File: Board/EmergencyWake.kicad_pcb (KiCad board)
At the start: 2 copper layers, 100 x 67 mm, 5 parts

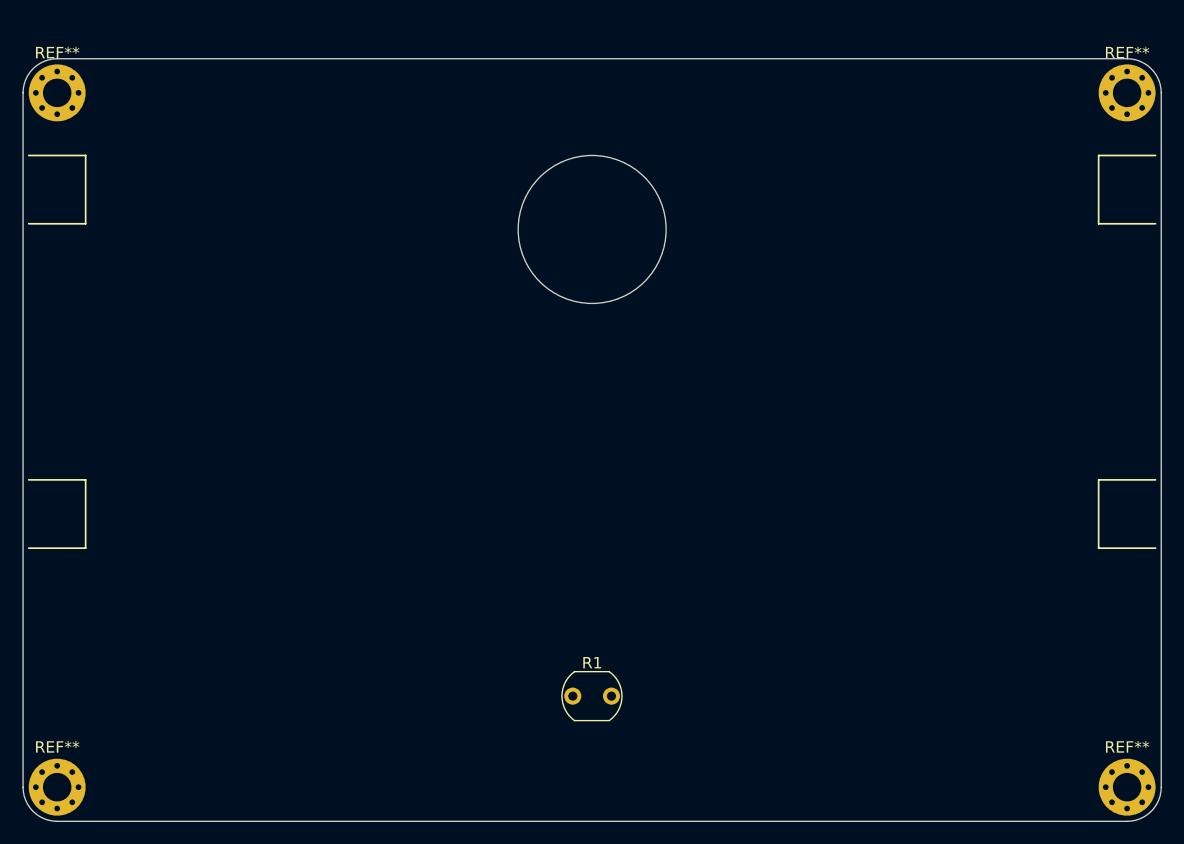
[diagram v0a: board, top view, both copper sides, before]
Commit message: [Board] Added a lot of main components
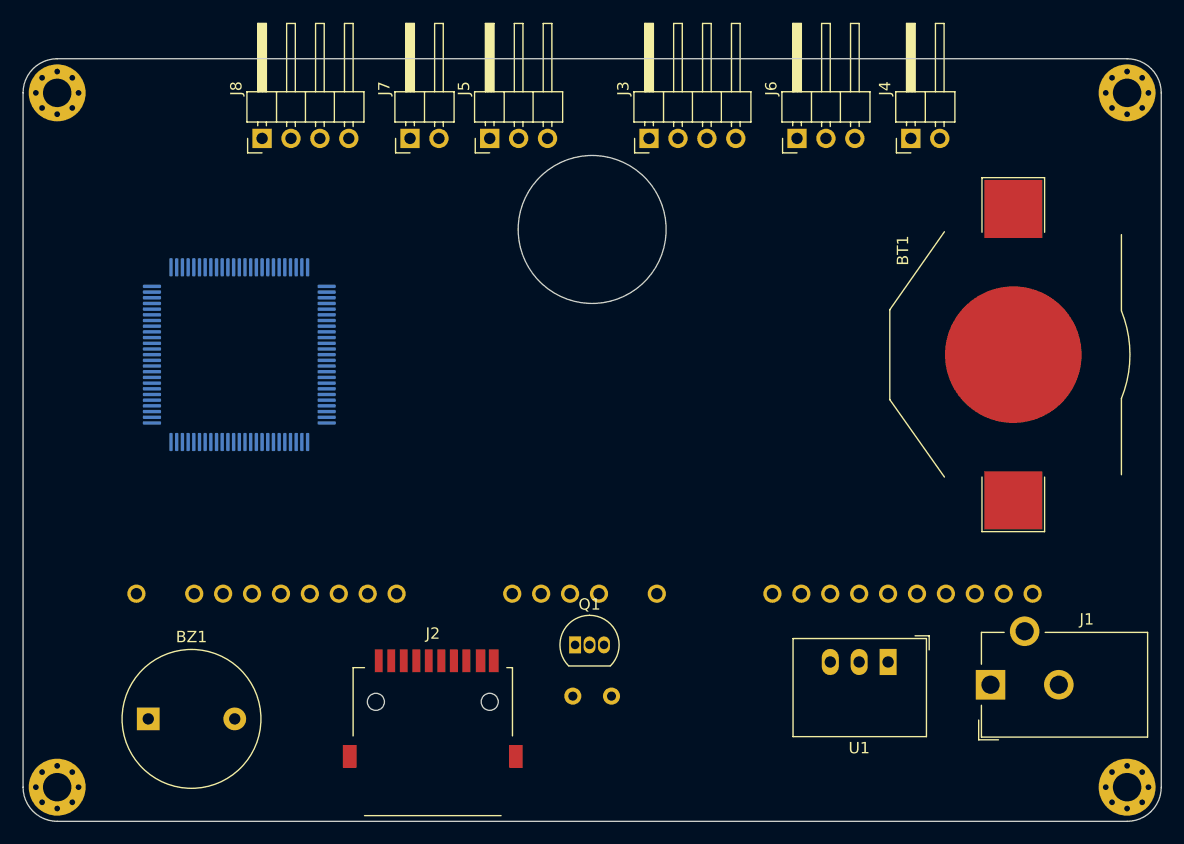
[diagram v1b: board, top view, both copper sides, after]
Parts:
- added BT1: Battery_Cell, Battery:BatteryHolder_Keystone_3002_1x2032, F.Cu at (187.0, 126.0)
- added BZ1: Buzzer, Buzzer_Beeper:Buzzer_12x9.5RM7.6, F.Cu at (111.0, 158.0)
- added D?1: FUTABA_4-LT-46ZB3, VFD:FUTABA_4-LT-46ZB3, B.Cu at (150.0, 126.0)
- added J1: Barrel_Jack_Switch, Connector_BarrelJack:BarrelJack_CUI_PJ-102AH_Horizontal, F.Cu at (185.0, 155.0)
- added J2: Micro_SD_Card_Det, Card:microSD_Attend_112I-TDAR-R 1, F.Cu at (136.0, 156.5)
- added J3: Conn_01x04, Connector_PinHeader_2.54mm:PinHeader_1x04_P2.54mm_Horizontal, F.Cu at (155.0, 107.0)
- added J4: Conn_01x02, Connector_PinHeader_2.54mm:PinHeader_1x02_P2.54mm_Horizontal, F.Cu at (178.0, 107.0)
- added J5: Conn_01x03, Connector_PinHeader_2.54mm:PinHeader_1x03_P2.54mm_Horizontal, F.Cu at (141.0, 107.0)
- added J6: Conn_01x03, Connector_PinHeader_2.54mm:PinHeader_1x03_P2.54mm_Horizontal, F.Cu at (168.0, 107.0)
- added J7: Conn_01x02, Connector_PinHeader_2.54mm:PinHeader_1x02_P2.54mm_Horizontal, F.Cu at (134.0, 107.0)
- added J8: Conn_01x04, Connector_PinHeader_2.54mm:PinHeader_1x04_P2.54mm_Horizontal, F.Cu at (121.0, 107.0)
- added Q1: MPSA13, Package_TO_SOT_THT:TO-92_Inline, F.Cu at (148.5, 151.5)
- added U1: R-78C3.3-1.0, Converter_DCDC:Converter_DCDC_RECOM_R-78E-0.5_THT, F.Cu at (176.0, 153.0)
- added U2: STM32F103VETx, Package_QFP:LQFP-100_14x14mm_P0.5mm, B.Cu at (119.0, 126.0)
- ? (x4): renamed from REF**; value MountingHole_2.5mm_Pad_Via -> (none)
- R1: moved to B.Cu

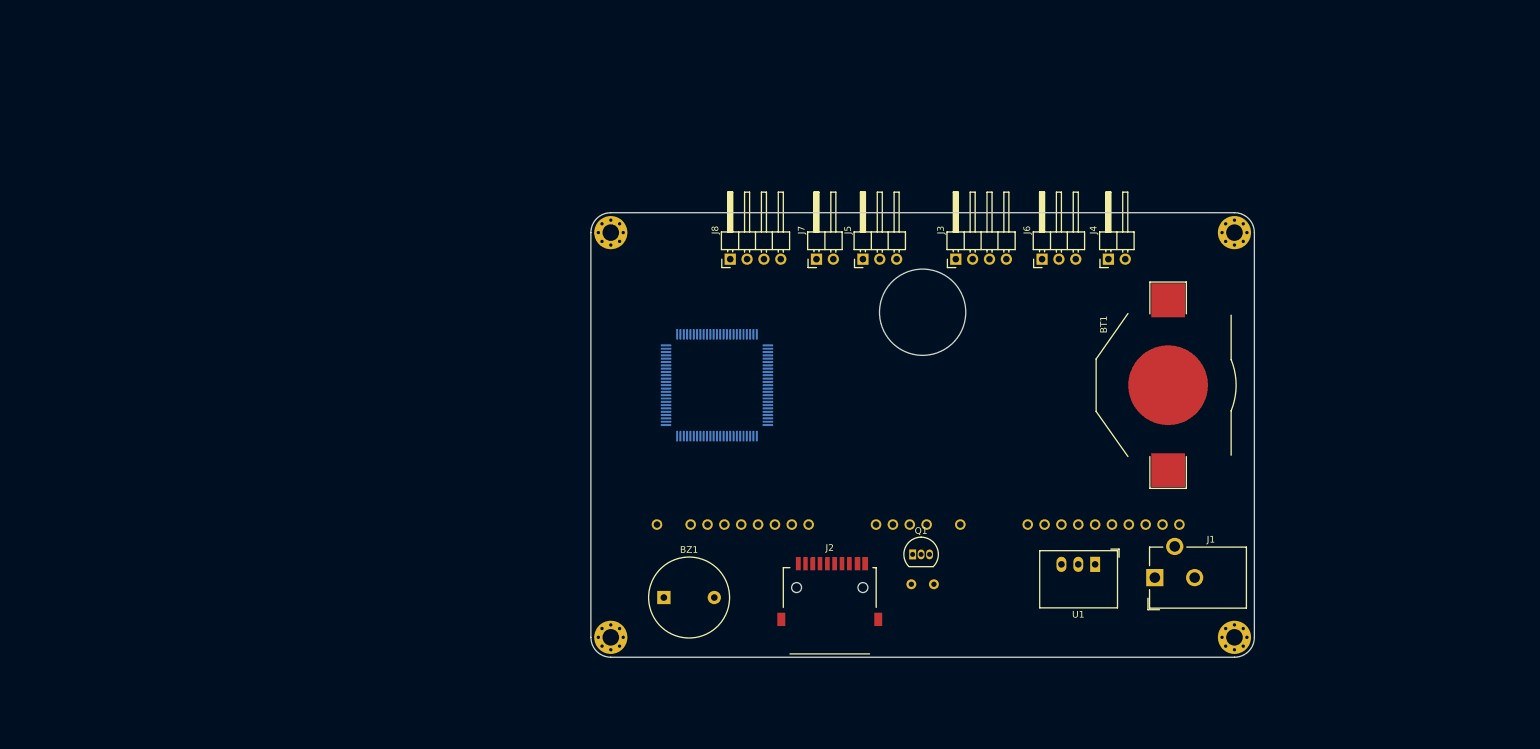
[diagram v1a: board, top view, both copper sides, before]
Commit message: [Board] Added all remaining components, arranged them approximately on PCB
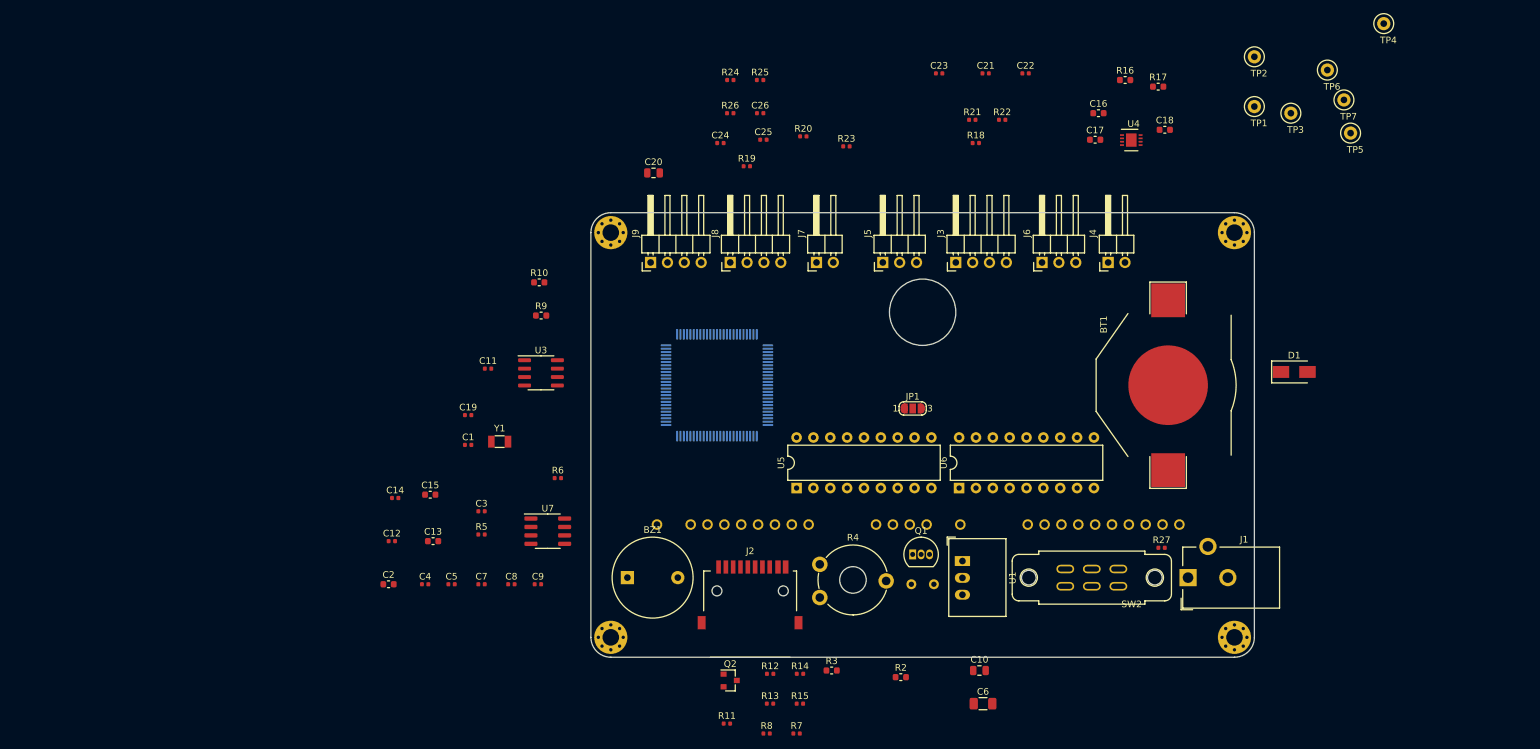
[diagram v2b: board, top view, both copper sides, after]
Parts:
- removed D?1: FUTABA_4-LT-46ZB3, VFD:FUTABA_4-LT-46ZB3
- added C1: 6p, Capacitor_SMD:C_0402_1005Metric, F.Cu at (81.5, 135.0)
- added C10: 22u,25V, Capacitor_SMD:C_0805_2012Metric, F.Cu at (158.6, 169.0)
- added C11: 100n, Capacitor_SMD:C_0402_1005Metric, F.Cu at (84.5, 123.5)
- added C12: 10n,50V, Capacitor_SMD:C_0402_1005Metric, F.Cu at (70.0, 149.5)
- added C13: 1u,50V, Capacitor_SMD:C_0603_1608Metric, F.Cu at (76.2, 149.5)
- added C14: 10n,50V, Capacitor_SMD:C_0402_1005Metric, F.Cu at (70.5, 143.0)
- added C15: 1u,50V, Capacitor_SMD:C_0603_1608Metric, F.Cu at (75.8, 142.5)
- added C16: 10n, Capacitor_SMD:C_0603_1608Metric, F.Cu at (176.5, 85.0)
- added C17: 10n, Capacitor_SMD:C_0603_1608Metric, F.Cu at (176.0, 89.0)
- added C18: 1u,50V, Capacitor_SMD:C_0603_1608Metric, F.Cu at (186.5, 87.5)
- added C19: 6p, Capacitor_SMD:C_0402_1005Metric, F.Cu at (81.5, 130.5)
- added C2: 4u7,16V, Capacitor_SMD:C_0603_1608Metric, F.Cu at (69.5, 156.0)
- added C20: 10u,50V, Capacitor_SMD:C_0805_2012Metric, F.Cu at (109.4, 94.0)
- added C21: 10n,50V, Capacitor_SMD:C_0402_1005Metric, F.Cu at (159.5, 79.0)
- added C22: 10n,50V, Capacitor_SMD:C_0402_1005Metric, F.Cu at (165.5, 79.0)
- added C23: 10n,50V, Capacitor_SMD:C_0402_1005Metric, F.Cu at (152.5, 79.0)
- added C24: 10n,50V, Capacitor_SMD:C_0402_1005Metric, F.Cu at (119.5, 89.5)
- added C25: 10n,50V, Capacitor_SMD:C_0402_1005Metric, F.Cu at (126.0, 89.0)
- added C26: 10n,50V, Capacitor_SMD:C_0402_1005Metric, F.Cu at (125.5, 85.0)
- added C3: 10n,50V, Capacitor_SMD:C_0402_1005Metric, F.Cu at (83.5, 145.0)
- added C4: 100n, Capacitor_SMD:C_0402_1005Metric, F.Cu at (75.0, 156.0)
- added C5: 100n, Capacitor_SMD:C_0402_1005Metric, F.Cu at (79.0, 156.0)
- added C6: 10u,50V, Capacitor_SMD:C_1206_3216Metric, F.Cu at (159.1, 174.0)
- added C7: 100n, Capacitor_SMD:C_0402_1005Metric, F.Cu at (83.5, 156.0)
- added C8: 100n, Capacitor_SMD:C_0402_1005Metric, F.Cu at (88.0, 156.0)
- added C9: 100n, Capacitor_SMD:C_0402_1005Metric, F.Cu at (92.0, 156.0)
- added D1: D_Schottky, Diode_SMD:D_SMA, F.Cu at (206.0, 124.0)
- added DISP1: FUTABA_4-LT-46ZB3, VFD:FUTABA_4-LT-46ZB3, B.Cu at (150.0, 126.0)
- added J9: Conn_01x04, Connector_PinHeader_2.54mm:PinHeader_1x04_P2.54mm_Horizontal, F.Cu at (109.0, 107.5)
- added JP1: SolderJumper_3_Open, Jumper:SolderJumper-3_P1.3mm_Open_RoundedPad1.0x1.5mm_NumberLabels, F.Cu at (148.5, 129.5)
- added Q2: AO3400A, Package_TO_SOT_SMD:SOT-23, F.Cu at (121.0, 170.5)
- added R10: 15k,1%, Resistor_SMD:R_0603_1608Metric, F.Cu at (92.2, 110.5)
- added R11: 100k, Resistor_SMD:R_0402_1005Metric, F.Cu at (120.5, 177.0)
- added R12: 100k, Resistor_SMD:R_0402_1005Metric, F.Cu at (127.0, 169.5)
- added R13: 100k, Resistor_SMD:R_0402_1005Metric, F.Cu at (127.0, 174.0)
- added R14: 100k, Resistor_SMD:R_0402_1005Metric, F.Cu at (131.5, 169.5)
- added R15: 100k, Resistor_SMD:R_0402_1005Metric, F.Cu at (131.5, 174.0)
- added R16: 300k, Resistor_SMD:R_0603_1608Metric, F.Cu at (180.5, 80.0)
- added R17: 300k, Resistor_SMD:R_0603_1608Metric, F.Cu at (185.5, 81.0)
- added R18: 100k, Resistor_SMD:R_0402_1005Metric, F.Cu at (158.0, 89.5)
- added R19: 10k, Resistor_SMD:R_0402_1005Metric, F.Cu at (123.5, 93.0)
- added R2: 27k, Resistor_SMD:R_0603_1608Metric, F.Cu at (146.7, 170.0)
- added R20: 10k, Resistor_SMD:R_0402_1005Metric, F.Cu at (132.0, 88.5)
- added R21: 100k, Resistor_SMD:R_0402_1005Metric, F.Cu at (157.5, 86.0)
- added R22: 100k, Resistor_SMD:R_0402_1005Metric, F.Cu at (162.0, 86.0)
- added R23: 100k, Resistor_SMD:R_0402_1005Metric, F.Cu at (138.5, 90.0)
- added R24: 100k, Resistor_SMD:R_0402_1005Metric, F.Cu at (121.0, 80.0)
- added R25: 100k, Resistor_SMD:R_0402_1005Metric, F.Cu at (125.5, 80.0)
- added R26: 100k, Resistor_SMD:R_0402_1005Metric, F.Cu at (121.0, 85.0)
- added R27: 100k, Resistor_SMD:R_0402_1005Metric, F.Cu at (186.0, 150.5)
- added R3: 4k7, Resistor_SMD:R_0603_1608Metric, F.Cu at (136.3, 169.0)
- added R4: 10k, Potentiometer_THT:Potentiometer_Piher_PT-10-V10_Vertical_Hole, F.Cu at (134.5, 158.0)
- added R5: 100k, Resistor_SMD:R_0402_1005Metric, F.Cu at (83.5, 148.5)
- added R6: 100k, Resistor_SMD:R_0402_1005Metric, F.Cu at (95.0, 140.0)
- added R7: 100k, Resistor_SMD:R_0402_1005Metric, F.Cu at (131.0, 178.5)
- added R8: 100k, Resistor_SMD:R_0402_1005Metric, F.Cu at (126.5, 178.5)
- added R9: 82k,1%, Resistor_SMD:R_0603_1608Metric, F.Cu at (92.5, 115.5)
- added SW2: SW_DPDT_x2, Switch:SlidingSwitch_6pin, F.Cu at (175.5, 155.0)
- added TP1: TestPoint, TestPoint:TestPoint_Loop_D1.80mm_Drill1.0mm_Beaded, F.Cu at (200.0, 84.0)
- added TP2: TestPoint, TestPoint:TestPoint_Loop_D1.80mm_Drill1.0mm_Beaded, F.Cu at (200.0, 76.5)
- added TP3: TestPoint, TestPoint:TestPoint_Loop_D1.80mm_Drill1.0mm_Beaded, F.Cu at (205.5, 85.0)
- added TP4: TestPoint, TestPoint:TestPoint_Loop_D1.80mm_Drill1.0mm_Beaded, F.Cu at (219.5, 71.5)
- added TP5: TestPoint, TestPoint:TestPoint_Loop_D1.80mm_Drill1.0mm_Beaded, F.Cu at (214.5, 88.0)
- added TP6: TestPoint, TestPoint:TestPoint_Loop_D1.80mm_Drill1.0mm_Beaded, F.Cu at (211.0, 78.5)
- added TP7: TestPoint, TestPoint:TestPoint_Loop_D1.80mm_Drill1.0mm_Beaded, F.Cu at (213.5, 83.0)
- added U3: M24C02-WMN, Package_SO:SOIC-8_3.9x4.9mm_P1.27mm, F.Cu at (92.5, 124.1)
- added U4: LM4670, Package_SON:WSON-8-1EP_3x3mm_P0.5mm_EP1.6x2.0mm, F.Cu at (181.4, 89.0)
- added U5: UDN6118A, Package_DIP:DIP-18_W7.62mm, F.Cu at (131.0, 141.5)
- added U6: UDN6118A, Package_DIP:DIP-18_W7.62mm, F.Cu at (155.5, 141.5)
- added U7: L9110S, Package_SO:SOP-8_3.76x4.96mm_P1.27mm, F.Cu at (93.5, 148.0)
- added Y1: 32,768, Crystal:Crystal_SMD_3215-2Pin_3.2x1.5mm, F.Cu at (86.2, 134.5)
- R1: value LDR07 -> GL5506
- U1: value R-78C3.3-1.0 -> Gaptec LME78_03-1.0
- moved U1 20.0 mm to (156.0, 152.5), turned to 270 degrees
- moved J2 12.0 mm to (124.0, 157.0)
- moved BZ1 6.26 mm to (105.5, 155.0)
- moved J1 5.00 mm to (190.0, 155.0)
- moved J5 3.04 mm to (144.0, 107.5)
- moved J4 0.50 mm to (178.0, 107.5)
- moved J3 0.50 mm to (155.0, 107.5)
- moved J6 0.50 mm to (168.0, 107.5)
- moved J7 0.50 mm to (134.0, 107.5)
- moved J8 0.50 mm to (121.0, 107.5)
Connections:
- net Net-(BZ1-Pad1) renamed /BUZZER
- net Net-(J2-Pad9) renamed /CARD_DET
- net Net-(J3-Pad2) renamed /SWCLK
- net Net-(J3-Pad3) renamed /SWDIO
- net Net-(J5-Pad1) renamed /UART_TX
- net Net-(J5-Pad2) renamed /UART_RX
- BT1 pad 1: Net-(BT1-Pad1) -> +3V0
- BT1 pad 2: Net-(BT1-Pad2) -> GND
- BZ1 pad 2: Net-(BZ1-Pad2) -> GND
- J1 pad 2: Net-(J1-Pad2) -> GND
- J2 pad 10: Net-(J2-Pad10) -> GND
- J2 pad 11: Net-(J2-Pad11) -> GND
- J2 pad 4: Net-(J2-Pad4) -> VCC
- J3 pad 1: Net-(J3-Pad1) -> VCC
- J3 pad 4: Net-(J3-Pad4) -> GND
- J4 pad 1: Net-(J4-Pad1) -> /SP+
- J4 pad 2: Net-(J4-Pad2) -> /SP-
- J5 pad 3: Net-(J5-Pad3) -> GND
- J6 pad 1: Net-(J6-Pad1) -> /TOGGLE_UP
- J6 pad 2: Net-(J6-Pad2) -> /TOGGLE_DOWN
- J6 pad 3: Net-(J6-Pad3) -> GND
- J7 pad 1: Net-(J7-Pad1) -> /LEVER
- J7 pad 2: Net-(J7-Pad2) -> GND
- J8 pad 3: Net-(J8-Pad3) -> /ENC_BUT
- J8 pad 4: Net-(J8-Pad4) -> GND
- Q1 pad 1: Net-(Q1-Pad1) -> +VDC
- Q1 pad 3: Net-(Q1-Pad3) -> +24V
- R1 pad 1: Net-(R1-Pad1) -> +24V
- R1 pad 2: Net-(R1-Pad2) -> Net-(Q1-Pad2)
- U1 pad 1: Net-(U1-Pad1) -> +24V
- U1 pad 2: Net-(U1-Pad2) -> GND
- U1 pad 3: Net-(U1-Pad3) -> VCC
- U2 pad 10: Net-(U2-Pad10) -> GND
- U2 pad 100: Net-(U2-Pad100) -> VCC
- U2 pad 11: Net-(U2-Pad11) -> VCC
- U2 pad 14: Net-(U2-Pad14) -> /RESET
- U2 pad 19: Net-(U2-Pad19) -> GND
- U2 pad 20: Net-(U2-Pad20) -> GND
- U2 pad 21: Net-(U2-Pad21) -> VCC
- U2 pad 22: Net-(U2-Pad22) -> VCC
- U2 pad 27: Net-(U2-Pad27) -> GND
- U2 pad 28: Net-(U2-Pad28) -> VCC
- U2 pad 49: Net-(U2-Pad49) -> GND
- U2 pad 50: Net-(U2-Pad50) -> VCC
- U2 pad 6: Net-(U2-Pad6) -> VCC
- U2 pad 74: Net-(U2-Pad74) -> GND
- U2 pad 75: Net-(U2-Pad75) -> VCC
- U2 pad 94: Net-(U2-Pad94) -> /BOOT0
- U2 pad 99: Net-(U2-Pad99) -> GND
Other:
- outline, holes or cut-outs redrawn

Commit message: [Board] Placed a lot of components!
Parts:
- added C27: 10n,50V, Capacitor_SMD:C_0402_1005Metric, B.Cu at (158.5, 92.5)
- added C28: 10n,50V, Capacitor_SMD:C_0402_1005Metric, B.Cu at (161.5, 92.5)
- added C29: 10n,50V, Capacitor_SMD:C_0402_1005Metric, B.Cu at (164.5, 92.5)
- added C30: 10n,50V, Capacitor_SMD:C_0402_1005Metric, B.Cu at (180.0, 89.0)
- added C31: 10n,50V, Capacitor_SMD:C_0402_1005Metric, B.Cu at (183.5, 89.0)
- added C32: 10n,50V, Capacitor_SMD:C_0402_1005Metric, B.Cu at (186.5, 89.0)
- added D2: white, LED_SMD:LED_0805_2012Metric_Castellated, B.Cu at (106.0, 132.0)
- added D3: white, LED_SMD:LED_0805_2012Metric_Castellated, B.Cu at (194.0, 126.0)
- added D4: white, LED_SMD:LED_0805_2012Metric_Castellated, B.Cu at (194.0, 132.0)
- added D5: SS54, Diode_SMD:D_SMA, B.Cu at (195.0, 147.0)
- added D6: SS54, Diode_SMD:D_SMA, B.Cu at (169.3, 153.5)
- added JP2: SolderJumper_3_Open, Jumper:SolderJumper-3_P1.3mm_Open_RoundedPad1.0x1.5mm_NumberLabels, F.Cu at (125.5, 140.0)
- added JP3: SolderJumper_3_Open, Jumper:SolderJumper-3_P1.3mm_Open_RoundedPad1.0x1.5mm_NumberLabels, F.Cu at (125.5, 143.0)
- added JP4: SolderJumper_3_Open, Jumper:SolderJumper-3_P1.3mm_Open_RoundedPad1.0x1.5mm_NumberLabels, F.Cu at (150.0, 140.0)
- added L1: 33u, Inductor_SMD:L_Wuerth_WE-PD-Typ-7345, B.Cu at (175.3, 154.5)
- added R28: 100k, Resistor_SMD:R_0402_1005Metric, B.Cu at (158.5, 89.5)
- added R29: 100k, Resistor_SMD:R_0402_1005Metric, B.Cu at (161.5, 89.5)
- added R30: 100k, Resistor_SMD:R_0402_1005Metric, B.Cu at (164.5, 89.5)
- added R31: 100k, Resistor_SMD:R_0402_1005Metric, B.Cu at (152.5, 95.0)
- added R32: 100k, Resistor_SMD:R_0402_1005Metric, B.Cu at (184.0, 92.0)
- added R33: 100k, Resistor_SMD:R_0402_1005Metric, B.Cu at (184.0, 94.5)
- added R34: 100k, Resistor_SMD:R_0402_1005Metric, B.Cu at (188.0, 94.5)
- added R35: 390, Resistor_SMD:R_0603_1608Metric, B.Cu at (226.5, 155.5)
- added R36: 390, Resistor_SMD:R_0603_1608Metric, B.Cu at (226.5, 159.5)
- added R37: 10k, Resistor_SMD:R_0603_1608Metric, B.Cu at (123.2, 95.0)
- added R38: 10k, Resistor_SMD:R_0603_1608Metric, B.Cu at (231.5, 155.0)
- added R39: 10k, Resistor_SMD:R_0603_1608Metric, B.Cu at (231.5, 159.0)
- added R40: 100k, Resistor_SMD:R_0402_1005Metric, B.Cu at (185.0, 149.0)
- added SW1: SW_DPDT_x2, Wuerth:452404020202, F.Cu at (184.0, 155.0)
- added SW3: SW_Push, Wuerth:436351045816, F.Cu at (160.0, 165.0)
- added SW4: SW_Push, Wuerth:436351045816, F.Cu at (150.0, 165.0)
- added TP10: -17V, TestPoint:TestPoint_Loop_D1.80mm_Drill1.0mm_Beaded, F.Cu at (21.0, 113.5)
- added TP11: TestPoint, TestPoint:TestPoint_Loop_D1.80mm_Drill1.0mm_Beaded, F.Cu at (17.0, 101.5)
- added TP8: -20V, TestPoint:TestPoint_Loop_D1.80mm_Drill1.0mm_Beaded, F.Cu at (14.5, 107.5)
- added TP9: LDR, TestPoint:TestPoint_Loop_D1.80mm_Drill1.0mm_Beaded, F.Cu at (150.0, 152.0)
- added U10: L9110S, Package_SO:SOP-8_3.76x4.96mm_P1.27mm, B.Cu at (233.5, 146.5)
- added U8: EL357N-G, Package_SO:SOP-4_3.8x4.1mm_P2.54mm, B.Cu at (224.5, 151.0)
- added U9: EL357N-G, Package_SO:SOP-4_3.8x4.1mm_P2.54mm, B.Cu at (224.5, 146.0)
- C1: value 6p -> 4u7,16V; footprint Capacitor_SMD:C_0402_1005Metric -> Capacitor_SMD:C_0603_1608Metric; moved to B.Cu
- C10: value 22u,25V -> 10n,50V; footprint Capacitor_SMD:C_0805_2012Metric -> Capacitor_SMD:C_0402_1005Metric; moved to B.Cu
- C11: value 100n -> 10n,50V; moved to B.Cu
- C12, C24, C25: value 10n,50V -> 1u,50V; footprint Capacitor_SMD:C_0402_1005Metric -> Capacitor_SMD:C_0603_1608Metric; moved to B.Cu
- C13: value 1u,50V -> 22u,25V; footprint Capacitor_SMD:C_0603_1608Metric -> Capacitor_SMD:C_0805_2012Metric; moved to B.Cu
- C14: value 10n,50V -> 100u,50V; footprint Capacitor_SMD:C_0402_1005Metric -> Capacitor_THT:CP_Radial_D6.3mm_P2.50mm
- C15: value 1u,50V -> 10n,50V; footprint Capacitor_SMD:C_0603_1608Metric -> Capacitor_SMD:C_0402_1005Metric; moved to B.Cu
- C16: value 10n -> 470p; moved to B.Cu
- C17: value 10n -> 1u,50V; moved to B.Cu
- C18: value 1u,50V -> 33u,63V; footprint Capacitor_SMD:C_0603_1608Metric -> Capacitor_THT:CP_Radial_D6.3mm_P2.50mm
- C19: value 6p -> 10n; footprint Capacitor_SMD:C_0402_1005Metric -> Capacitor_SMD:C_0603_1608Metric; moved to B.Cu
- C2: value 4u7,16V -> 100n; footprint Capacitor_SMD:C_0603_1608Metric -> Capacitor_SMD:C_0402_1005Metric; moved to B.Cu
- C20: value 10u,50V -> 10n; footprint Capacitor_SMD:C_0805_2012Metric -> Capacitor_SMD:C_0603_1608Metric; moved to B.Cu
- C21, C22: value 10n,50V -> 6p; moved to B.Cu
- C23: value 10n,50V -> 100n; moved to B.Cu
- C26: value 10n,50V -> 10u,50V; footprint Capacitor_SMD:C_0402_1005Metric -> Capacitor_SMD:C_0805_2012Metric; moved to B.Cu
- C3, C4, C5, C7, C8, R11, R12, R13, R14, R15, R6, R8, Y1: moved to B.Cu
- C6: value 10u,50V -> 100n; footprint Capacitor_SMD:C_1206_3216Metric -> Capacitor_SMD:C_0402_1005Metric; moved to B.Cu
- C9: value 100n -> 10u,50V; footprint Capacitor_SMD:C_0402_1005Metric -> Capacitor_SMD:C_1206_3216Metric; moved to B.Cu
- D1: value D_Schottky -> white; footprint Diode_SMD:D_SMA -> LED_SMD:LED_0805_2012Metric_Castellated; moved to B.Cu
- J1: value Barrel_Jack_Switch -> USB_C_Plug_USB2.0; footprint Connector_BarrelJack:BarrelJack_CUI_PJ-102AH_Horizontal -> Wuerth:632723300011
- J3: value Conn_01x04 -> Conn_01x03; footprint Connector_PinHeader_2.54mm:PinHeader_1x04_P2.54mm_Horizontal -> Connector_PinHeader_2.54mm:PinHeader_1x03_P2.54mm_Horizontal
- J6: value Conn_01x03 -> Conn_01x04; footprint Connector_PinHeader_2.54mm:PinHeader_1x03_P2.54mm_Horizontal -> Connector_PinHeader_2.54mm:PinHeader_1x04_P2.54mm_Horizontal
- Q1: value MPSA13 -> AO3400A; footprint Package_TO_SOT_THT:TO-92_Inline -> Package_TO_SOT_SMD:SOT-23; moved to B.Cu
- Q2: value AO3400A -> AO3401A; moved to B.Cu
- R1: value GL5506 -> 100k; footprint OptoDevice:R_LDR_5.1x4.3mm_P3.4mm_Vertical -> Resistor_SMD:R_0402_1005Metric
- R10: value 15k,1% -> 100k; footprint Resistor_SMD:R_0603_1608Metric -> Resistor_SMD:R_0402_1005Metric; moved to B.Cu
- R16, R17: value 300k -> 100k; footprint Resistor_SMD:R_0603_1608Metric -> Resistor_SMD:R_0402_1005Metric; moved to B.Cu
- R18: value 100k -> 0.18; footprint Resistor_SMD:R_0402_1005Metric -> Wuerth:561070332057; moved to B.Cu
- R19: value 10k -> 75k; footprint Resistor_SMD:R_0402_1005Metric -> Resistor_SMD:R_0603_1608Metric; moved to B.Cu
- R2: value 27k -> 150; footprint Resistor_SMD:R_0603_1608Metric -> Resistor_SMD:R_0402_1005Metric; moved to B.Cu
- R20: value 10k -> 5.1k; footprint Resistor_SMD:R_0402_1005Metric -> Resistor_SMD:R_0603_1608Metric; moved to B.Cu
- R21, R22: value 100k -> 300k; footprint Resistor_SMD:R_0402_1005Metric -> Resistor_SMD:R_0603_1608Metric; moved to B.Cu
- R23: value 100k -> 20k; footprint Resistor_SMD:R_0402_1005Metric -> Resistor_SMD:R_0603_1608Metric; moved to B.Cu
- R24: value 100k -> GL5516; footprint Resistor_SMD:R_0402_1005Metric -> OptoDevice:R_LDR_5.1x4.3mm_P3.4mm_Vertical; moved to B.Cu
- R25: value 100k -> R; footprint Resistor_SMD:R_0402_1005Metric -> Resistor_SMD:R_0603_1608Metric; moved to B.Cu
- R26, R27: value 100k -> 10k; moved to B.Cu
- R3: value 4k7 -> 150; footprint Resistor_SMD:R_0603_1608Metric -> Resistor_SMD:R_0402_1005Metric; moved to B.Cu
- R4: value 10k -> 150; footprint Potentiometer_THT:Potentiometer_Piher_PT-10-V10_Vertical_Hole -> Resistor_SMD:R_0402_1005Metric; moved to B.Cu
- R5: value 100k -> 150; moved to B.Cu
- R7: value 100k -> 1.5k; moved to B.Cu
- R9: value 82k,1% -> 100k; footprint Resistor_SMD:R_0603_1608Metric -> Resistor_SMD:R_0402_1005Metric; moved to B.Cu
- SW2: value SW_DPDT_x2 -> SW_Push; footprint Switch:SlidingSwitch_6pin -> Wuerth:436351045816
- TP1: value TestPoint -> 5V in
- TP2: value TestPoint -> GND in
- TP3: value TestPoint -> 5V
- TP4: value TestPoint -> 3V
- TP5: value TestPoint -> DCDC in
- TP6: value TestPoint -> GND
- TP7: value TestPoint -> Audio
- U1: value Gaptec LME78_03-1.0 -> M24C02-WMN; footprint Converter_DCDC:Converter_DCDC_RECOM_R-78E-0.5_THT -> Package_SO:SOIC-8_3.9x4.9mm_P1.27mm; moved to B.Cu
- U2: value STM32F103VETx -> AMS1117-3.3; footprint Package_QFP:LQFP-100_14x14mm_P0.5mm -> Package_TO_SOT_SMD:SOT-223-3_TabPin2
- U3: value M24C02-WMN -> MC34063AD; moved to B.Cu
- U4: value LM4670 -> STM32F103VETx; footprint Package_SON:WSON-8-1EP_3x3mm_P0.5mm_EP1.6x2.0mm -> Package_QFP:LQFP-100_14x14mm_P0.5mm; moved to B.Cu
- U5: value UDN6118A -> LM4670; footprint Package_DIP:DIP-18_W7.62mm -> Package_SON:WSON-8-1EP_3x3mm_P0.5mm_EP1.6x2.0mm; moved to B.Cu
- U6: value UDN6118A -> AMS1117-3.3; footprint Package_DIP:DIP-18_W7.62mm -> Package_TO_SOT_SMD:SOT-223-3_TabPin2; moved to B.Cu
- U7: value L9110S -> PT6312B; footprint Package_SO:SOP-8_3.76x4.96mm_P1.27mm -> Package_QFP:LQFP-44_10x10mm_P0.8mm; moved to B.Cu
- moved TP4 210.1 mm to (19.5, 136.0)
- moved TP5 199.1 mm to (17.0, 113.5)
- moved TP7 196.8 mm to (24.0, 136.0)
- moved TP6 194.9 mm to (22.5, 128.0)
- moved TP3 185.4 mm to (23.5, 120.5)
- moved C25 119.9 mm to (235.0, 139.0)
- moved R5 112.0 mm to (194.0, 130.3)
- moved D1 100.0 mm to (106.0, 126.0)
- moved C17 96.3 mm to (94.3, 140.0), turned to 180 degrees
- moved R6 94.5 mm to (188.0, 157.0), turned to 270 degrees
- moved R16 93.9 mm to (120.2, 152.0), turned to 90 degrees
- moved C14 91.4 mm to (160.6, 158.3)
- moved TP2 86.1 mm to (203.0, 162.5)
- moved C22 85.8 mm to (85.5, 110.0)
- moved U7 84.4 mm to (175.0, 126.0), turned to 315 degrees
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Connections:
- net Net-(J2-Pad5) renamed /SD_CK_SCK
- net Net-(J2-Pad7) renamed /SD_D0_MISO
- C1 pad 1: Net-(C1-Pad1) -> VCC
- C11 pad 1: VCC -> /USR_BUT
- C14 pad 1: VCC -> +5V
- C16 pad 2: /AUDIO_OUT -> -VDC
- C17 pad 1: GND -> VCC
- C17 pad 2: Net-(C17-Pad2) -> GND
- C18 pad 1: VCC -> GND
- C18 pad 2: GND -> -VDC
- C19 pad 2: GND -> /AUDIO_OUT
- C20 pad 1: VCC -> GND
- C20 pad 2: GND -> Net-(C20-Pad2)
- C21 pad 1: GND -> Net-(C21-Pad1)
- C21 pad 2: /LEVER -> GND
- C22 pad 1: GND -> Net-(C22-Pad1)
- C22 pad 2: /TOGGLE_UP -> GND
- C23 pad 1: GND -> VCC
- C23 pad 2: /TOGGLE_DOWN -> GND
- C24 pad 1: Net-(C24-Pad1) -> VCC
- C25 pad 1: Net-(C25-Pad1) -> Vdrive
- C25 pad 2: GND -> -VDC
- C26 pad 1: GND -> VCC
- C26 pad 2: /ENC_BUT -> GND
- C6 pad 1: +24V -> VCC
- C9 pad 1: VCC -> +5V
- D1 pad 1: VCC -> GND
- DISP1 pad 9: Net-(DISP1-Pad9) -> /SEG_L
- J2 pad 2: Net-(J2-Pad2) -> /SD_CS
- J2 pad 3: Net-(J2-Pad3) -> /SD_CMD_MOSI
- J2 pad 9: /CARD_DET -> /SD_DET
- J3 pad 1: VCC -> /TOGGLE_UP
- J3 pad 2: /SWCLK -> /TOGGLE_DOWN
- J3 pad 3: /SWDIO -> GND
- J4 pad 1: /SP+ -> /LEVER
- J4 pad 2: /SP- -> GND
- J6 pad 1: /TOGGLE_UP -> VCC
- J6 pad 2: /TOGGLE_DOWN -> GND
- J6 pad 3: GND -> /DCF_PON
- J7 pad 1: /LEVER -> /SP+
- J7 pad 2: GND -> /SP-
- J8 pad 1: Net-(C24-Pad1) -> Net-(J8-Pad1)
- J8 pad 2: Net-(C25-Pad1) -> /SWCLK
- J8 pad 3: /ENC_BUT -> /SWDIO
- J9 pad 1: VCC -> Net-(C30-Pad1)
- J9 pad 2: GND -> Net-(C31-Pad1)
- J9 pad 3: /DCF_PON -> /ENC_BUT
- J9 pad 4: /DCF_SIG -> GND
- JP1 pad 1: /VFD_GRID_2_HV -> /SD_CMD
- JP1 pad 2: Net-(DISP1-Pad17) -> /SD_CMD_MOSI
- JP1 pad 3: +VDC -> /SD_MOSI
- Q1 pad 1: +VDC -> /SD_EN
- Q1 pad 2: Net-(Q1-Pad2) -> GND
- Q1 pad 3: +24V -> Net-(J2-Pad6)
- Q2 pad 1: /CARD_EN -> /DCDC_EN
- Q2 pad 2: GND -> +5V
- Q2 pad 3: Net-(J2-Pad6) -> Net-(Q2-Pad3)
- R1 pad 1: +24V -> VCC
- R1 pad 2: Net-(Q1-Pad2) -> /RESET
- R10 pad 1: /V_SENSE -> VCC
- R10 pad 2: GND -> /SD_CS
- R11 pad 1: /CARD_EN -> /SD_EN
- R12 pad 2: Net-(J2-Pad3) -> /SD_CMD_MOSI
- R15 pad 2: Net-(J2-Pad8) -> /USR_BUT
- R16 pad 1: Net-(C16-Pad1) -> VCC
- R16 pad 2: Net-(R16-Pad2) -> Net-(J2-Pad8)
- R17 pad 1: Net-(C17-Pad2) -> +5V
- R17 pad 2: Net-(R17-Pad2) -> /DCDC_EN
- R18 pad 1: /LEVER -> Net-(Q2-Pad3)
- R18 pad 2: VCC -> Net-(R18-Pad2)
- R19 pad 1: /ENC_A -> GND
- R19 pad 2: Net-(C24-Pad1) -> Net-(R19-Pad2)
- R2 pad 1: +24V -> /LED1
- R2 pad 2: Net-(Q1-Pad2) -> Net-(D1-Pad2)
- R20 pad 1: /ENC_B -> Net-(R19-Pad2)
- R20 pad 2: Net-(C25-Pad1) -> -VDC
- R21 pad 1: /TOGGLE_UP -> Net-(C19-Pad1)
- R21 pad 2: VCC -> Net-(R21-Pad2)
- R22 pad 1: /TOGGLE_DOWN -> Net-(C20-Pad2)
- R22 pad 2: VCC -> Net-(R22-Pad2)
- R23 pad 1: /DCF_PON -> VCC
- R23 pad 2: VCC -> Net-(R23-Pad2)
- R24 pad 1: VCC -> Net-(R23-Pad2)
- R24 pad 2: Net-(C24-Pad1) -> GND
- R25 pad 1: VCC -> Net-(R25-Pad1)
- R25 pad 2: Net-(C25-Pad1) -> VCC
- R26 pad 1: /ENC_BUT -> /ENC_A
- R26 pad 2: VCC -> Net-(C30-Pad1)
- R27 pad 1: +VDC -> /ENC_B
- R27 pad 2: Net-(DISP1-Pad2) -> Net-(C31-Pad1)
- R3 pad 1: Net-(Q1-Pad2) -> /LED2
- R3 pad 2: Net-(R3-Pad2) -> Net-(D2-Pad2)
- R4 pad 1: Net-(R4-Pad1) -> /LED3
- R4 pad 2: Net-(R3-Pad2) -> Net-(D3-Pad2)
- R5 pad 1: VCC -> /LED4
- R5 pad 2: /RESET -> Net-(D4-Pad2)
- R6 pad 1: /BOOT0 -> Net-(J1-PadA5)
- R7 pad 1: VCC -> /USB_DP
- R7 pad 2: Net-(J2-Pad1) -> VCC
- R8 pad 1: VCC -> /BOOT0
- R8 pad 2: Net-(J2-Pad2) -> GND
- R9 pad 1: +24V -> VCC
- R9 pad 2: /V_SENSE -> Net-(J2-Pad1)
- SW2 pad 1: +24V -> GND
- SW2 pad 2: Net-(J1-Pad1) -> /RESET
- TP1 pad 1: +VDC -> Net-(J1-PadA4)
- TP2 pad 1: +24V -> GND
- TP3 pad 1: /V_SENSE -> +5V
- TP5 pad 1: GND -> Net-(Q2-Pad3)
- TP6 pad 1: /AUDIO_OUT -> GND
- TP7 pad 1: /DCF_PON -> /AUDIO_OUT
- U1 pad 1: +24V -> GND
- U1 pad 3: VCC -> GND
- U2 pad 1: Net-(U2-Pad1) -> GND
- U2 pad 2: Net-(U2-Pad2) -> VCC
- U2 pad 3: Net-(U2-Pad3) -> +5V
- U3 pad 1: GND -> Net-(R18-Pad2)
- U3 pad 2: GND -> Net-(D6-Pad1)
- U3 pad 3: GND -> Net-(C16-Pad1)
- U3 pad 4: GND -> -VDC
- U3 pad 5: /EEPROM_SDA -> Net-(R19-Pad2)
- U3 pad 6: /EEPROM_SCL -> Net-(Q2-Pad3)
- U3 pad 7: /EEPROM_NWC -> Net-(R18-Pad2)
- U3 pad 8: VCC -> Net-(R18-Pad2)
- U4 pad 1: /AUDIO_EN -> /ENC_BUT
- U4 pad 2: Net-(R16-Pad2) -> /TOGGLE_UP
- U4 pad 3: Net-(R17-Pad2) -> /TOGGLE_DOWN
- U4 pad 4: GND -> /USR_BUT
- U4 pad 5: /SP+ -> Net-(U4-Pad5)
- U4 pad 6: GND -> VCC
- U4 pad 7: VCC -> Net-(U4-Pad7)
- U4 pad 8: /SP- -> Net-(C22-Pad1)
- U4 pad 9: (no net) -> Net-(C21-Pad1)
- U5 pad 1: /VFD_SEG_A -> /AUDIO_EN
- U5 pad 2: /VFD_SEG_B -> Net-(R21-Pad2)
- U5 pad 3: /VFD_SEG_C -> Net-(R22-Pad2)
- U5 pad 4: /VFD_SEG_D -> GND
- U5 pad 5: /VFD_SEG_E -> /SP+
- U5 pad 6: /VFD_SEG_F -> GND
- U5 pad 7: /VFD_SEG_G -> VCC
- U5 pad 8: /VFD_DP -> /SP-
- U5 pad 9: GND -> (no net)
- U6 pad 1: /VFD_NO_1 -> -VDC
- U6 pad 2: /VFD_NO_2 -> Vdrive
- U6 pad 3: /VFD_NO_3 -> GND
- U7 pad 1: Net-(DISP1-Pad1) -> Net-(U7-Pad1)
- U7 pad 2: VCC -> Net-(U7-Pad2)
- U7 pad 3: VCC -> Net-(U7-Pad3)
- U7 pad 4: Net-(DISP1-Pad32) -> Net-(U7-Pad4)
- U7 pad 5: GND -> /VFD_DOUT
- U7 pad 6: /VFD_FIL+ -> /VFD_DIN
- U7 pad 7: /VFD_FIL- -> GND
- U7 pad 8: GND -> /VFD_CLK
- Y1 pad 1: Net-(C1-Pad1) -> Net-(C21-Pad1)
- Y1 pad 2: Net-(C19-Pad1) -> Net-(C22-Pad1)
